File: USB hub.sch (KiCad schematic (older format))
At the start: 48 parts, among them IC1 FE1.1S, IC2 24SN, J1 USB_A_SMT_FEMALE, J2 USB_A_SMT_FEMALE, J3 USB_A_SMT_FEMALE, J4 USB_C2-LAYER, X1 12MHz

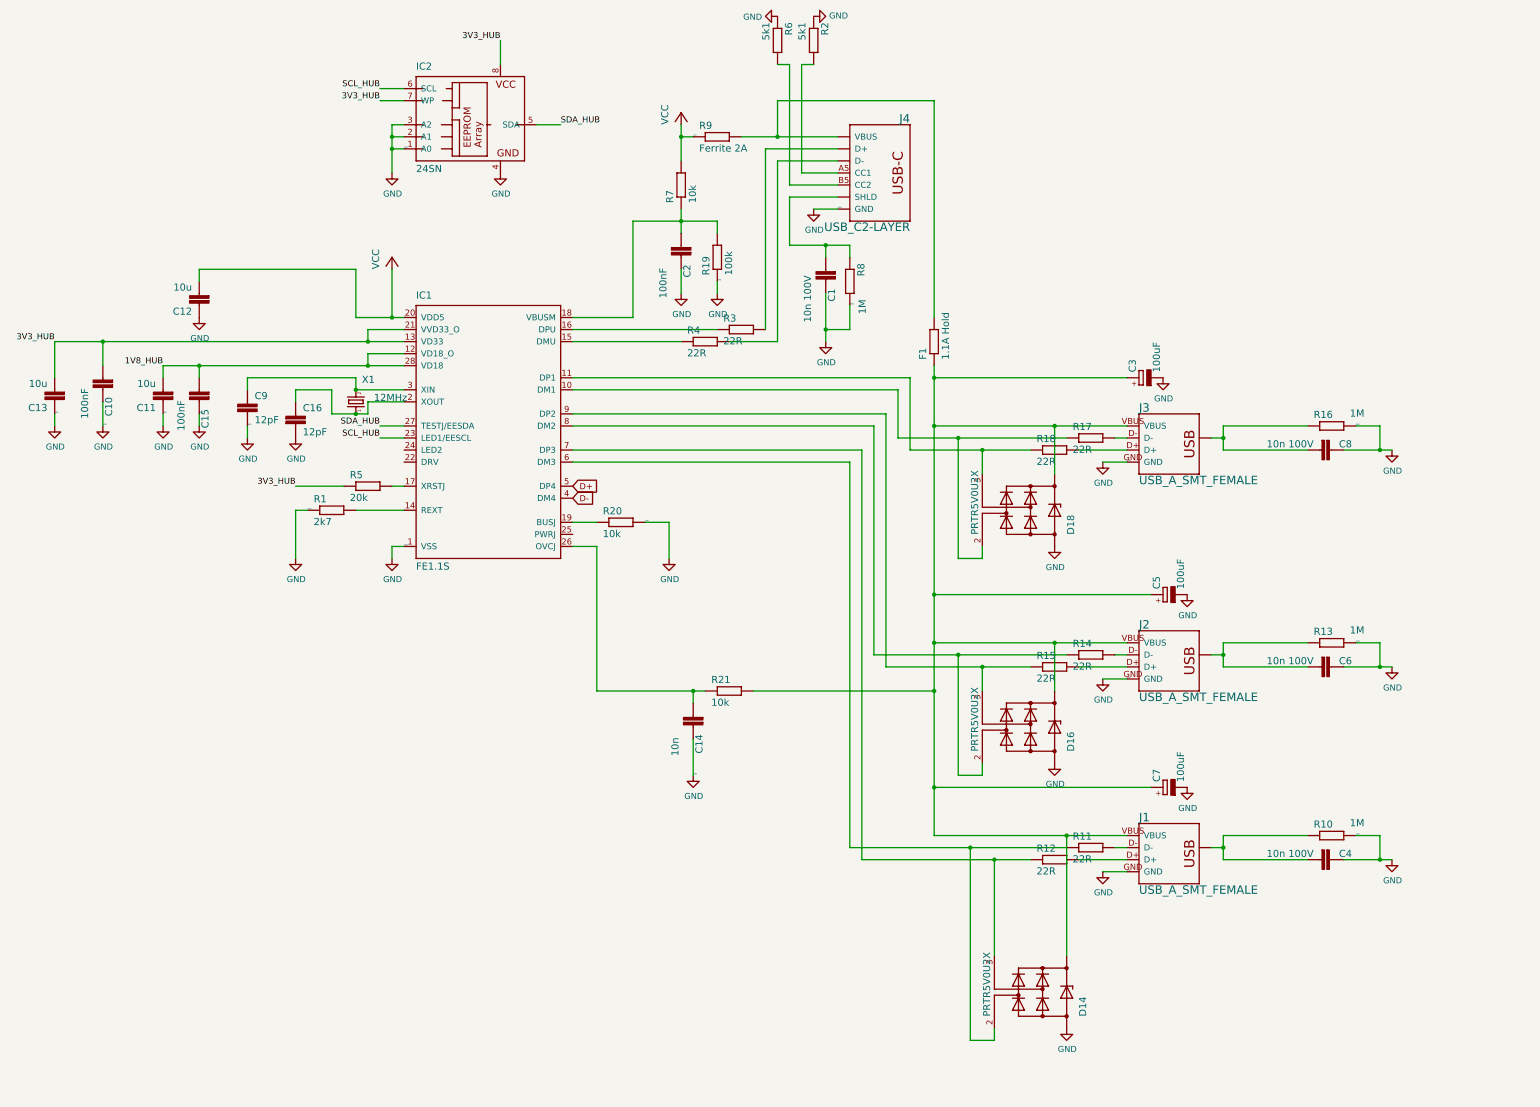
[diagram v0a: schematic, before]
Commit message: Begin annotation
Annotated schematic and began associating symbols with footprints.
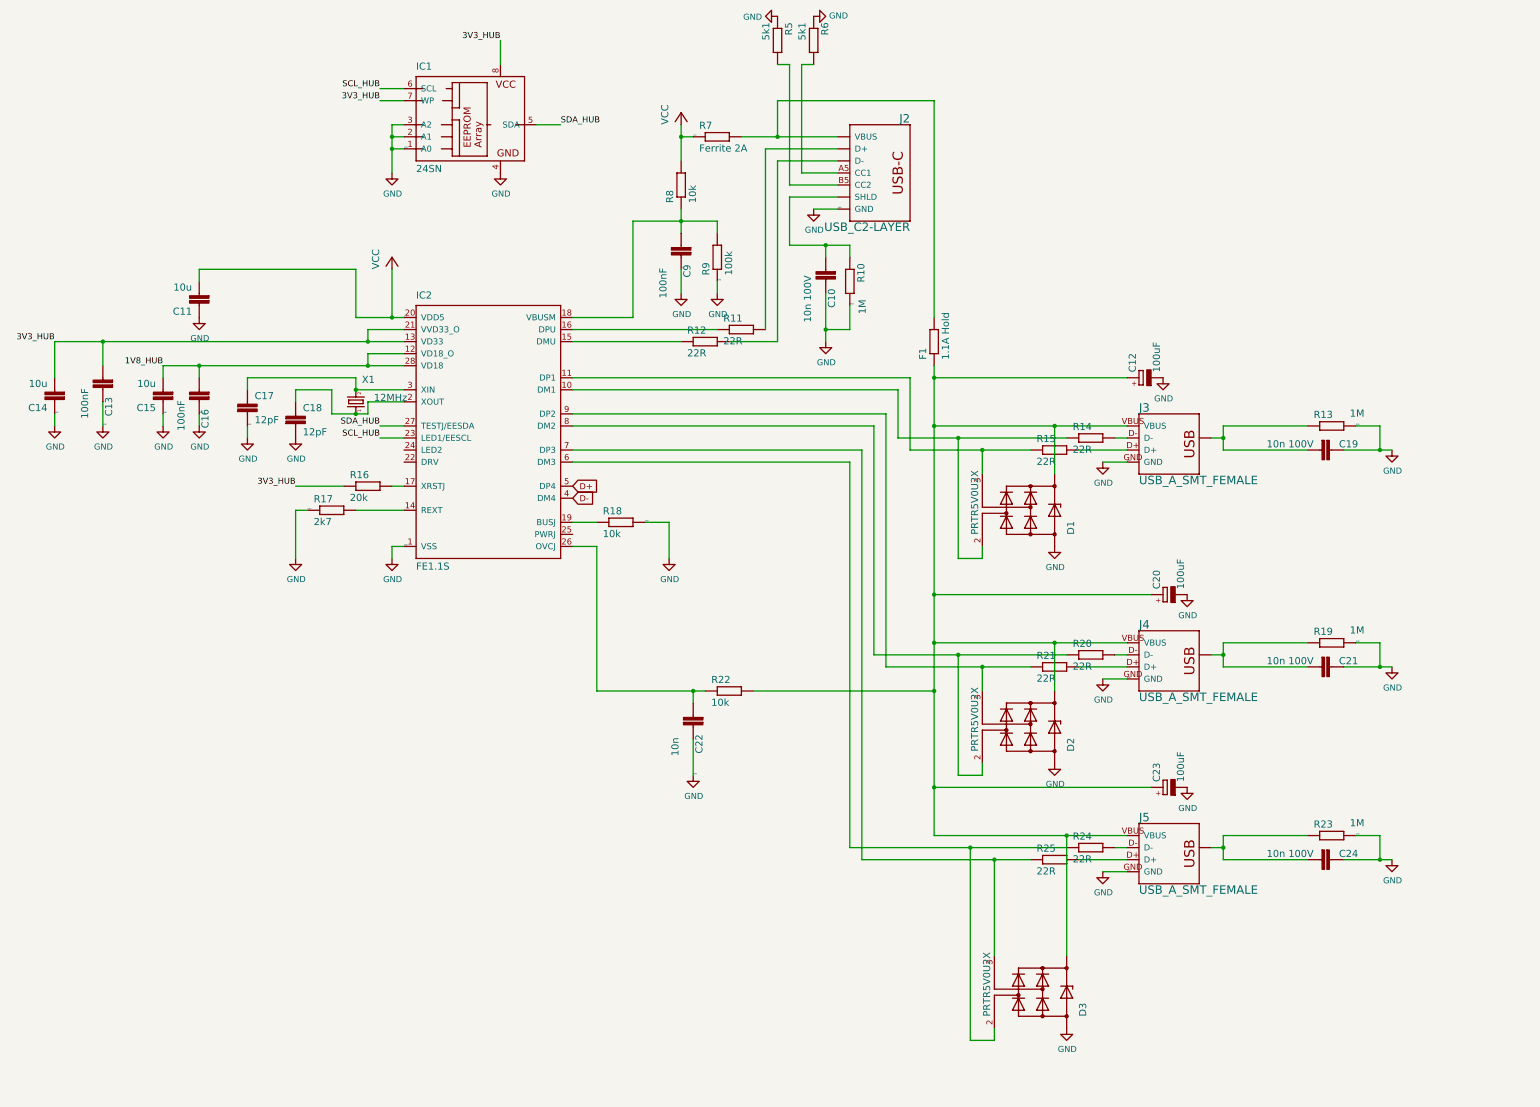
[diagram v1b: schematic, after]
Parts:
- C10: renamed from C1; footprint hub_keyboard:C0603 -> Capacitor_SMD:C_0805_2012Metric
- C11: renamed from C12; footprint hub_keyboard:C0603 -> Capacitor_SMD:C_0805_2012Metric
- C12: renamed from C3; footprint hub_keyboard:CT3528 -> Capacitor_SMD:C_0805_2012Metric
- C13: renamed from C10; footprint hub_keyboard:C0603 -> Capacitor_SMD:C_0805_2012Metric
- C14: renamed from C13; footprint hub_keyboard:C0603 -> Capacitor_SMD:C_0805_2012Metric
- C15: renamed from C11; footprint hub_keyboard:C0603 -> Capacitor_SMD:C_0805_2012Metric
- C16: renamed from C15; footprint hub_keyboard:C0603 -> Capacitor_SMD:C_0805_2012Metric
- C17: renamed from C9; footprint hub_keyboard:C0603 -> Capacitor_SMD:C_0805_2012Metric
- C18: renamed from C16; footprint hub_keyboard:C0603 -> Capacitor_SMD:C_0805_2012Metric
- C19: renamed from C8; footprint hub_keyboard:C0603 -> Capacitor_SMD:C_0805_2012Metric
- C20: renamed from C5; footprint hub_keyboard:CT3528 -> Capacitor_SMD:C_0805_2012Metric
- C21: renamed from C6; footprint hub_keyboard:C0603 -> Capacitor_SMD:C_0805_2012Metric
- C22: renamed from C14; footprint hub_keyboard:C0603 -> Capacitor_SMD:C_0805_2012Metric
- C23: renamed from C7; footprint hub_keyboard:CT3528 -> Capacitor_SMD:C_0805_2012Metric
- C24: renamed from C4; footprint hub_keyboard:C0603 -> Capacitor_SMD:C_0805_2012Metric
- C9: renamed from C2; footprint hub_keyboard:C0603 -> Capacitor_SMD:C_0805_2012Metric
- renumbered D18 to D1, D16 to D2, D14 to D3, IC2 to IC1, IC1 to IC2, J4 to J2, J2 to J4, J1 to J5, R8 to R10, R3 to R11, R4 to R12, R16 to R13, R17 to R14, R18 to R15, R5 to R16, R1 to R17, R20 to R18, R13 to R19, R14 to R20, R15 to R21, R21 to R22, R10 to R23, R11 to R24, R12 to R25, R6 to R5, R2 to R6, R9 to R7, R7 to R8, R19 to R9

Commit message: Assign Footprints
Continued assigning footprints
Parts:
- D1, D2, D3: footprint hub_keyboard:SOT143 -> Keyboard Footprints:SOT143B
- F1: footprint hub_keyboard:R1210 -> Fuse:Fuse_1206_3216Metric
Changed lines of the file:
@@
 F 0 "F1" H 8150 3659 59  0000 L BNN
 F 1 "1.1A Hold" H 8150 3470 59  0000 L BNN
-F 2 "hub_keyboard:R1210" H 8300 3600 50  0001 C CNN
+F 2 "Fuse:Fuse_1206_3216Metric" H 8300 3600 50  0001 C CNN
 F 3 "" H 8300 3600 50  0001 C CNN
 F 4 "TRUE" H 8300 3600 59  0001 L BNN "EXTENDED"
@@
 F 0 "D1" H 8797 5400 59  0000 L BNN
 F 1 "PRTR5V0U2X" H 8797 4603 59  0000 L BNN
-F 2 "hub_keyboard:SOT143" H 9000 5000 50  0001 C CNN
+F 2 "Keyboard Footprints:SOT143B" H 9000 5000 50  0001 C CNN
 F 3 "" H 9000 5000 50  0001 C CNN
 F 4 "1727-3884-1-ND" H 9000 5000 59  0001 L BNN "DIGIKEY"
@@
 F 0 "D2" H 8797 7200 59  0000 L BNN
 F 1 "PRTR5V0U2X" H 8797 6403 59  0000 L BNN
-F 2 "hub_keyboard:SOT143" H 9000 6800 50  0001 C CNN
+F 2 "Keyboard Footprints:SOT143B" H 9000 6800 50  0001 C CNN
 F 3 "" H 9000 6800 50  0001 C CNN
 F 4 "1727-3884-1-ND" H 9000 6800 59  0001 L BNN "DIGIKEY"
@@
 F 0 "D3" H 8898 9400 59  0000 L BNN
 F 1 "PRTR5V0U2X" H 8898 8603 59  0000 L BNN
-F 2 "hub_keyboard:SOT143" H 9100 9000 50  0001 C CNN
+F 2 "Keyboard Footprints:SOT143B" H 9100 9000 50  0001 C CNN
 F 3 "" H 9100 9000 50  0001 C CNN
 F 4 "1727-3884-1-ND" H 9100 9000 59  0001 L BNN "DIGIKEY"

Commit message: Associate FP
added debounce to encoder. finalized footrpint association.
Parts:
- R10, R11, R12, R13, R14, R15, R16, R17, R18, R19, R20, R21, R22, R23, R24, R25, R5, R6, R8, R9: footprint hub_keyboard:R0603 -> 1_Keyboard Footprints:R_0603
- X1: footprint hub_keyboard:3.2X2.5_KX-7 -> Crystal:Crystal_SMD_0603-2Pin_6.0x3.5mm
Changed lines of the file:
@@
 F 0 "R13" H 11450 4359 59  0000 L BNN
 F 1 "1M" H 11750 4370 59  0000 L BNN
-F 2 "hub_keyboard:R0603" H 11600 4300 50  0001 C CNN
+F 2 "1_Keyboard Footprints:R_0603" H 11600 4300 50  0001 C CNN
 F 3 "" H 11600 4300 50  0001 C CNN
 F 4 "C22935" H 11600 4300 59  0001 L BNN "LCSC"
@@
 F 0 "R19" H 11450 6159 59  0000 L BNN
 F 1 "1M" H 11750 6170 59  0000 L BNN
-F 2 "hub_keyboard:R0603" H 11600 6100 50  0001 C CNN
+F 2 "1_Keyboard Footprints:R_0603" H 11600 6100 50  0001 C CNN
 F 3 "" H 11600 6100 50  0001 C CNN
 F 4 "C22935" H 11600 6100 59  0001 L BNN "LCSC"
@@
 F 0 "R23" H 11450 7759 59  0000 L BNN
 F 1 "1M" H 11750 7770 59  0000 L BNN
-F 2 "hub_keyboard:R0603" H 11600 7700 50  0001 C CNN
+F 2 "1_Keyboard Footprints:R_0603" H 11600 7700 50  0001 C CNN
 F 3 "" H 11600 7700 50  0001 C CNN
 F 4 "C22935" H 11600 7700 59  0001 L BNN "LCSC"
@@
 F 0 "R10" H 7450 3159 59  0000 L BNN
 F 1 "1M" H 7750 3170 59  0000 L BNN
-F 2 "hub_keyboard:R0603" H 7600 3100 50  0001 C CNN
+F 2 "1_Keyboard Footprints:R_0603" H 7600 3100 50  0001 C CNN
 F 3 "" H 7600 3100 50  0001 C CNN
 F 4 "C22935" H 7600 3100 59  0001 L BNN "LCSC"
@@
 F 0 "R11" H 6550 3559 59  0000 L BNN
 F 1 "22R" H 6550 3370 59  0000 L BNN
-F 2 "hub_keyboard:R0603" H 6700 3500 50  0001 C CNN
+F 2 "1_Keyboard Footprints:R_0603" H 6700 3500 50  0001 C CNN
 F 3 "" H 6700 3500 50  0001 C CNN
 F 4 "C23345" H 6700 3500 59  0001 L BNN "LCSC"
@@
 F 0 "R12" H 6250 3659 59  0000 L BNN
 F 1 "22R" H 6250 3470 59  0000 L BNN
-F 2 "hub_keyboard:R0603" H 6400 3600 50  0001 C CNN
+F 2 "1_Keyboard Footprints:R_0603" H 6400 3600 50  0001 C CNN
 F 3 "" H 6400 3600 50  0001 C CNN
 F 4 "C23345" H 6400 3600 59  0001 L BNN "LCSC"
@@
 F 0 "R17" H 3150 5059 59  0000 L BNN
 F 1 "2k7" H 3150 4870 59  0000 L BNN
-F 2 "hub_keyboard:R0603" H 3300 5000 50  0001 C CNN
+F 2 "1_Keyboard Footprints:R_0603" H 3300 5000 50  0001 C CNN
 F 3 "" H 3300 5000 50  0001 C CNN
 F 4 "C13167" H 3300 5000 59  0001 L BNN "LCSC"
@@
 F 0 "R18" H 5550 5159 59  0000 L BNN
 F 1 "10k" H 5550 4970 59  0000 L BNN
-F 2 "hub_keyboard:R0603" H 5700 5100 50  0001 C CNN
+F 2 "1_Keyboard Footprints:R_0603" H 5700 5100 50  0001 C CNN
 F 3 "" H 5700 5100 50  0001 C CNN
 F 4 "C25804" H 5700 5100 59  0001 L BNN "LCSC"
@@
 F 0 "X1" V 3650 4050 59  0000 R TNN
 F 1 "12MHz" V 3500 3950 59  0000 R TNN
-F 2 "hub_keyboard:3.2X2.5_KX-7" H 3500 4100 50  0001 C CNN
+F 2 "Crystal:Crystal_SMD_0603-2Pin_6.0x3.5mm" H 3500 4100 50  0001 C CNN
 F 3 "" H 3500 4100 50  0001 C CNN
 F 4 "C9002" H 3500 4100 59  0001 L BNN "LCSC"
@@
 F 0 "R16" H 3450 4859 59  0000 L BNN
 F 1 "20k" H 3450 4670 59  0000 L BNN
-F 2 "hub_keyboard:R0603" H 3600 4800 50  0001 C CNN
+F 2 "1_Keyboard Footprints:R_0603" H 3600 4800 50  0001 C CNN
 F 3 "" H 3600 4800 50  0001 C CNN
 F 4 "C4184" H 3600 4800 59  0001 L BNN "LCSC"
@@
 F 0 "R8" H 6050 2359 59  0000 L BNN
 F 1 "10k" H 6050 2170 59  0000 L BNN
-F 2 "hub_keyboard:R0603" H 6200 2300 50  0001 C CNN
+F 2 "1_Keyboard Footprints:R_0603" H 6200 2300 50  0001 C CNN
 F 3 "" H 6200 2300 50  0001 C CNN
 F 4 "C25804" H 6200 2300 59  0001 L BNN "LCSC"
@@
 F 0 "R9" H 6350 2959 59  0000 L BNN
 F 1 "100k" H 6350 2770 59  0000 L BNN
-F 2 "hub_keyboard:R0603" H 6500 2900 50  0001 C CNN
+F 2 "1_Keyboard Footprints:R_0603" H 6500 2900 50  0001 C CNN
 F 3 "" H 6500 2900 50  0001 C CNN
 F 4 "C25803" H 6500 2900 59  0001 L BNN "LCSC"
@@
 F 0 "R22" H 6450 6559 59  0000 L BNN
 F 1 "10k" H 6450 6370 59  0000 L BNN
-F 2 "hub_keyboard:R0603" H 6600 6500 50  0001 C CNN
+F 2 "1_Keyboard Footprints:R_0603" H 6600 6500 50  0001 C CNN
 F 3 "" H 6600 6500 50  0001 C CNN
 F 4 "C25804" H 6600 6500 59  0001 L BNN "LCSC"
@@
 F 0 "R6" H 7150 1159 59  0000 L BNN
 F 1 "5k1" H 7150 970 59  0000 L BNN
-F 2 "hub_keyboard:R0603" H 7300 1100 50  0001 C CNN
+F 2 "1_Keyboard Footprints:R_0603" H 7300 1100 50  0001 C CNN
 F 3 "" H 7300 1100 50  0001 C CNN
 F 4 "C23186" H 7300 1100 59  0001 L BNN "LCSC"
@@
 F 0 "R5" H 6850 1159 59  0000 L BNN
 F 1 "5k1" H 6850 970 59  0000 L BNN
-F 2 "hub_keyboard:R0603" H 7000 1100 50  0001 C CNN
+F 2 "1_Keyboard Footprints:R_0603" H 7000 1100 50  0001 C CNN
 F 3 "" H 7000 1100 50  0001 C CNN
 F 4 "C23186" H 7000 1100 59  0001 L BNN "LCSC"
@@
 F 0 "R14" H 9450 4459 59  0000 L BNN
 F 1 "22R" H 9450 4270 59  0000 L BNN
-F 2 "hub_keyboard:R0603" H 9600 4400 50  0001 C CNN
+F 2 "1_Keyboard Footprints:R_0603" H 9600 4400 50  0001 C CNN
 F 3 "" H 9600 4400 50  0001 C CNN
 F 4 "C23345" H 9600 4400 59  0001 L BNN "LCSC"
@@
 F 0 "R15" H 9150 4559 59  0000 L BNN
 F 1 "22R" H 9150 4370 59  0000 L BNN
-F 2 "hub_keyboard:R0603" H 9300 4500 50  0001 C CNN
+F 2 "1_Keyboard Footprints:R_0603" H 9300 4500 50  0001 C CNN
 F 3 "" H 9300 4500 50  0001 C CNN
 F 4 "C23345" H 9300 4500 59  0001 L BNN "LCSC"
@@
 F 0 "R20" H 9450 6259 59  0000 L BNN
 F 1 "22R" H 9450 6070 59  0000 L BNN
-F 2 "hub_keyboard:R0603" H 9600 6200 50  0001 C CNN
+F 2 "1_Keyboard Footprints:R_0603" H 9600 6200 50  0001 C CNN
 F 3 "" H 9600 6200 50  0001 C CNN
 F 4 "C23345" H 9600 6200 59  0001 L BNN "LCSC"
@@
 F 0 "R21" H 9150 6359 59  0000 L BNN
 F 1 "22R" H 9150 6170 59  0000 L BNN
-F 2 "hub_keyboard:R0603" H 9300 6300 50  0001 C CNN
+F 2 "1_Keyboard Footprints:R_0603" H 9300 6300 50  0001 C CNN
 F 3 "" H 9300 6300 50  0001 C CNN
 F 4 "C23345" H 9300 6300 59  0001 L BNN "LCSC"
@@
 F 0 "R24" H 9450 7859 59  0000 L BNN
 F 1 "22R" H 9450 7670 59  0000 L BNN
-F 2 "hub_keyboard:R0603" H 9600 7800 50  0001 C CNN
+F 2 "1_Keyboard Footprints:R_0603" H 9600 7800 50  0001 C CNN
 F 3 "" H 9600 7800 50  0001 C CNN
 F 4 "C23345" H 9600 7800 59  0001 L BNN "LCSC"
@@
 F 0 "R25" H 9150 7959 59  0000 L BNN
 F 1 "22R" H 9150 7770 59  0000 L BNN
-F 2 "hub_keyboard:R0603" H 9300 7900 50  0001 C CNN
+F 2 "1_Keyboard Footprints:R_0603" H 9300 7900 50  0001 C CNN
 F 3 "" H 9300 7900 50  0001 C CNN
 F 4 "C23345" H 9300 7900 59  0001 L BNN "LCSC"

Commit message: Fixed symbols
Re-wired MCU XTAL and corrected footprints
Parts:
- C12, C20, C23: footprint Capacitor_SMD:C_0805_2012Metric -> hub_keyboard:CT3528
- D1, D2, D3: footprint Keyboard Footprints:SOT143B -> hub_keyboard:SOT143
- X1: footprint Crystal:Crystal_SMD_0603-2Pin_6.0x3.5mm -> Crystal:Crystal_SMD_3225-4Pin_3.2x2.5mm
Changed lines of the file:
@@
 F 0 "X1" V 3650 4050 59  0000 R TNN
 F 1 "12MHz" V 3500 3950 59  0000 R TNN
-F 2 "Crystal:Crystal_SMD_0603-2Pin_6.0x3.5mm" H 3500 4100 50  0001 C CNN
+F 2 "Crystal:Crystal_SMD_3225-4Pin_3.2x2.5mm" H 3500 4100 50  0001 C CNN
 F 3 "" H 3500 4100 50  0001 C CNN
 F 4 "C9002" H 3500 4100 59  0001 L BNN "LCSC"
@@
 F 0 "C12" H 10045 3919 59  0000 L BNN
 F 1 "100uF" H 10045 3719 59  0000 L BNN
-F 2 "Capacitor_SMD:C_0805_2012Metric" H 10000 3900 50  0001 C CNN
+F 2 "hub_keyboard:CT3528" H 10000 3900 50  0001 C CNN
 F 3 "" H 10000 3900 50  0001 C CNN
 F 4 "C16133" H 10000 3900 59  0001 L BNN "LCSC"
@@
 F 0 "C20" H 10245 5719 59  0000 L BNN
 F 1 "100uF" H 10245 5519 59  0000 L BNN
-F 2 "Capacitor_SMD:C_0805_2012Metric" H 10200 5700 50  0001 C CNN
+F 2 "hub_keyboard:CT3528" H 10200 5700 50  0001 C CNN
 F 3 "" H 10200 5700 50  0001 C CNN
 F 4 "C16133" H 10200 5700 59  0001 L BNN "LCSC"
@@
 F 0 "C23" H 10245 7319 59  0000 L BNN
 F 1 "100uF" H 10245 7119 59  0000 L BNN
-F 2 "Capacitor_SMD:C_0805_2012Metric" H 10200 7300 50  0001 C CNN
+F 2 "hub_keyboard:CT3528" H 10200 7300 50  0001 C CNN
 F 3 "" H 10200 7300 50  0001 C CNN
 F 4 "C16133" H 10200 7300 59  0001 L BNN "LCSC"
@@
 F 0 "D1" H 8797 5400 59  0000 L BNN
 F 1 "PRTR5V0U2X" H 8797 4603 59  0000 L BNN
-F 2 "Keyboard Footprints:SOT143B" H 9000 5000 50  0001 C CNN
+F 2 "hub_keyboard:SOT143" H 9000 5000 50  0001 C CNN
 F 3 "" H 9000 5000 50  0001 C CNN
 F 4 "1727-3884-1-ND" H 9000 5000 59  0001 L BNN "DIGIKEY"
@@
 F 0 "D2" H 8797 7200 59  0000 L BNN
 F 1 "PRTR5V0U2X" H 8797 6403 59  0000 L BNN
-F 2 "Keyboard Footprints:SOT143B" H 9000 6800 50  0001 C CNN
+F 2 "hub_keyboard:SOT143" H 9000 6800 50  0001 C CNN
 F 3 "" H 9000 6800 50  0001 C CNN
 F 4 "1727-3884-1-ND" H 9000 6800 59  0001 L BNN "DIGIKEY"
@@
 F 0 "D3" H 8898 9400 59  0000 L BNN
 F 1 "PRTR5V0U2X" H 8898 8603 59  0000 L BNN
-F 2 "Keyboard Footprints:SOT143B" H 9100 9000 50  0001 C CNN
+F 2 "hub_keyboard:SOT143" H 9100 9000 50  0001 C CNN
 F 3 "" H 9100 9000 50  0001 C CNN
 F 4 "1727-3884-1-ND" H 9100 9000 59  0001 L BNN "DIGIKEY"
